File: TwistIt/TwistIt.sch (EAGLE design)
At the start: 13 parts

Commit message: Fix small things for Servo and Twistit
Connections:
- net P2: now also R2.1
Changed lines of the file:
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@@
 <segment>
 <pinref part="ST1" gate="G$1" pin="P$3"/>
-<wire x1="139.7" y1="99.06" x2="129.54" y2="99.06" width="0.1524" layer="91"/>
+<wire x1="139.7" y1="99.06" x2="121.92" y2="99.06" width="0.1524" layer="91"/>
 <label x="137.16" y="99.06" size="1.778" layer="95"/>
+<pinref part="R2" gate="G$1" pin="1"/>
 </segment>
 <segment>

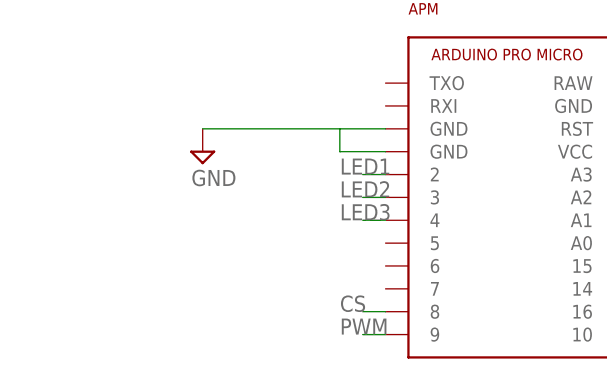
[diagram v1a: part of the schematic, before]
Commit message: Add encoder, start adding bom info to library
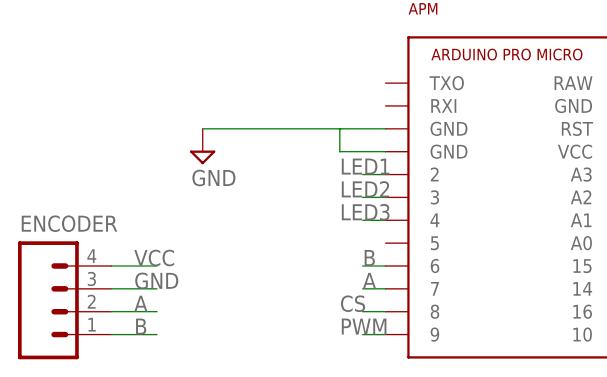
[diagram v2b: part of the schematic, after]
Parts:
- added ENCODER: (no value), pie:M041X04-MTA
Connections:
- new net A: APM.7, ENCODER.2
- new net B: APM.6, ENCODER.1
- net GND: now also ENCODER.3
- net VCC: now also ENCODER.4
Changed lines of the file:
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@@
 <part name="R6" library="pie" deviceset="R-US_" device="R0603" value="330"/>
 <part name="SUPPLY6" library="pie" deviceset="GND" device=""/>
+<part name="ENCODER" library="pie" deviceset="M04" device="1X04-MTA"/>
 </parts>
 <sheets>
@@
 <instance part="R6" gate="G$1" x="99.06" y="139.7"/>
 <instance part="SUPPLY6" gate="GND" x="111.76" y="137.16"/>
+<instance part="ENCODER" gate="G$1" x="10.16" y="83.82"/>
 </instances>
 <busses>
@@
 <wire x1="104.14" y1="139.7" x2="111.76" y2="139.7" width="0.1524" layer="91"/>
 </segment>
+<segment>
+<pinref part="ENCODER" gate="G$1" pin="3"/>
+<wire x1="17.78" y1="83.82" x2="22.86" y2="83.82" width="0.1524" layer="91"/>
+<label x="20.32" y="83.82" size="1.778" layer="95"/>
+</segment>
 </net>
 <net name="P1" class="0">
@@
 <wire x1="139.7" y1="142.24" x2="134.62" y2="142.24" width="0.1524" layer="91"/>
 </segment>
+<segment>
+<pinref part="ENCODER" gate="G$1" pin="4"/>
+<wire x1="17.78" y1="86.36" x2="22.86" y2="86.36" width="0.1524" layer="91"/>
+<label x="20.32" y="86.36" size="1.778" layer="95"/>
+</segment>
 </net>
 <net name="P2" class="0">
@@
 </segment>
 </net>
+<net name="A" class="0">
+<segment>
+<pinref part="ENCODER" gate="G$1" pin="2"/>
+<wire x1="17.78" y1="81.28" x2="22.86" y2="81.28" width="0.1524" layer="91"/>
+<label x="20.32" y="81.28" size="1.778" layer="95"/>
+</segment>
+<segment>
+<pinref part="APM" gate="G$1" pin="7"/>
+<wire x1="48.26" y1="83.82" x2="45.72" y2="83.82" width="0.1524" layer="91"/>
+<label x="45.72" y="83.82" size="1.778" layer="95"/>
+</segment>
+</net>
+<net name="B" class="0">
+<segment>
+<pinref part="ENCODER" gate="G$1" pin="1"/>
+<wire x1="17.78" y1="78.74" x2="22.86" y2="78.74" width="0.1524" layer="91"/>
+<label x="20.32" y="78.74" size="1.778" layer="95"/>
+</segment>
+<segment>
+<pinref part="APM" gate="G$1" pin="6"/>
+<wire x1="48.26" y1="86.36" x2="45.72" y2="86.36" width="0.1524" layer="91"/>
+<label x="45.72" y="86.36" size="1.778" layer="95"/>
+</segment>
+</net>

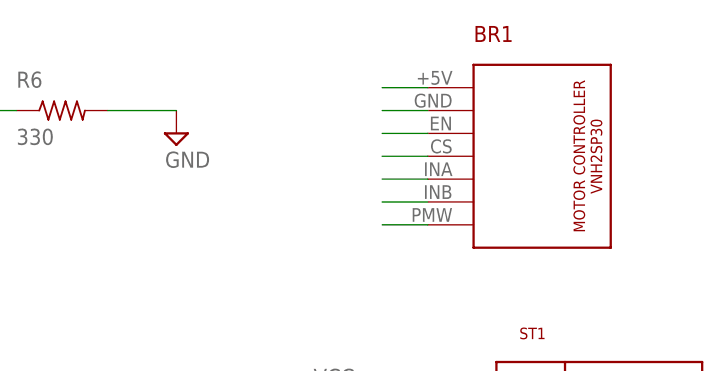
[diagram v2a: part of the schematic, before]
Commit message: Add more info to lbr; remove 5V from motor controlle rbreakout on twistit
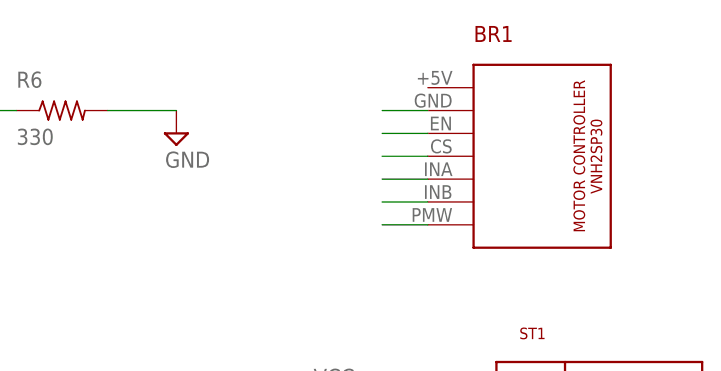
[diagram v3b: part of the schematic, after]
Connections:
- net VCC: no longer BR1.+5V
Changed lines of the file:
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@@
-</segment>
-<segment>
-<pinref part="BR1" gate="G$1" pin="+5V"/>
-<wire x1="139.7" y1="142.24" x2="134.62" y2="142.24" width="0.1524" layer="91"/>
 </segment>
 <segment>

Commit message: Readd the 5V rail on vhns
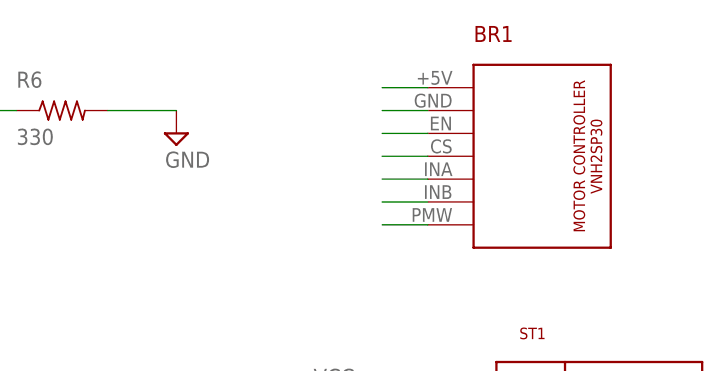
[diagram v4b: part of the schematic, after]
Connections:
- net VCC: now also BR1.+5V
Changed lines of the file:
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@@
 <label x="20.32" y="86.36" size="1.778" layer="95"/>
+</segment>
+<segment>
+<pinref part="BR1" gate="G$1" pin="+5V"/>
+<wire x1="139.7" y1="142.24" x2="134.62" y2="142.24" width="0.1524" layer="91"/>
 </segment>
 </net>

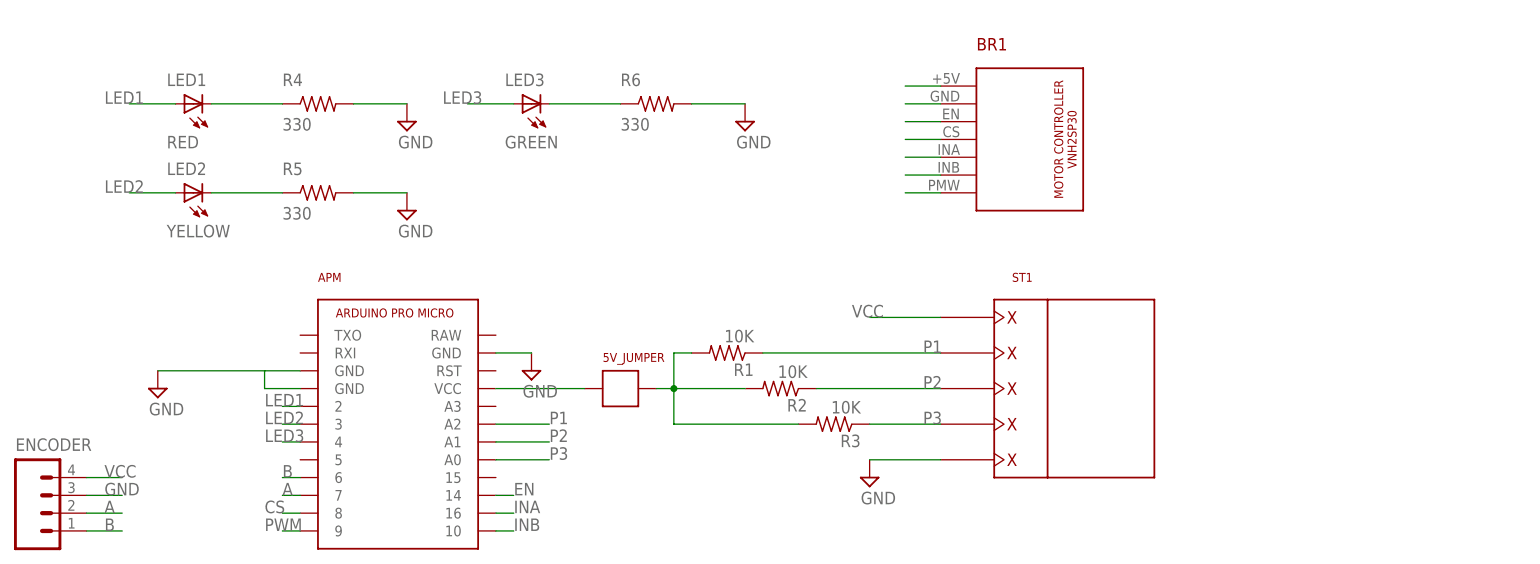
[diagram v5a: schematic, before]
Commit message: Rearange encoder to account for pullout and update parts
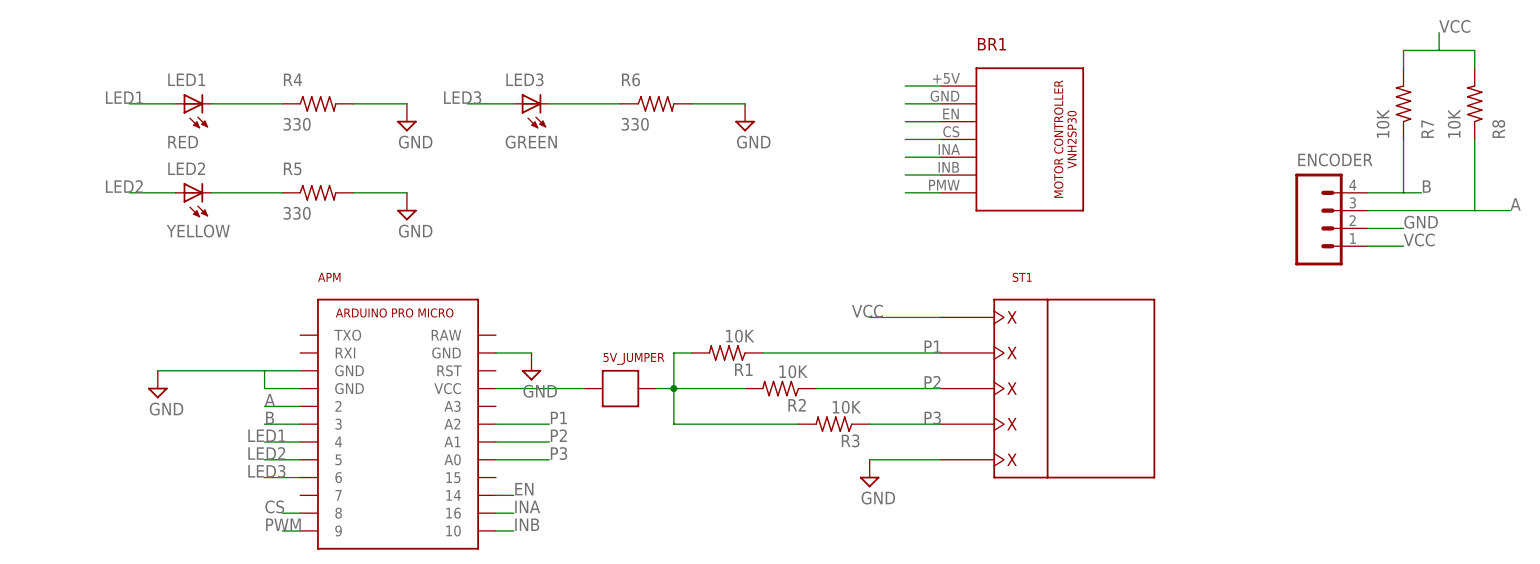
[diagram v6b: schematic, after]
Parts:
- added R7, R8: 10K, pie:R-US_R0603
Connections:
- net A: now also APM.2, ENCODER.3, R8.1; no longer APM.7, ENCODER.2
- net B: now also APM.3, ENCODER.4, R7.1; no longer APM.6, ENCODER.1
- net GND: now also ENCODER.2; no longer ENCODER.3
- net LED1: now also APM.4; no longer APM.2
- net LED2: now also APM.5; no longer APM.3
- net LED3: now also APM.6; no longer APM.4
- net VCC: now also ENCODER.1, R7.2, R8.2; no longer ENCODER.4
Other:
- moved on the sheet: ENCODER
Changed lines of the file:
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@@
 <part name="SUPPLY6" library="pie" deviceset="GND" device=""/>
 <part name="ENCODER" library="pie" deviceset="M04" device="1X04-MTA"/>
+<part name="R7" library="pie" deviceset="R-US_" device="R0603" value="10K"/>
+<part name="R8" library="pie" deviceset="R-US_" device="R0603" value="10K"/>
 </parts>
 <sheets>
@@
 <instance part="R6" gate="G$1" x="99.06" y="139.7"/>
 <instance part="SUPPLY6" gate="GND" x="111.76" y="137.16"/>
-<instance part="ENCODER" gate="G$1" x="10.16" y="83.82"/>
+<instance part="ENCODER" gate="G$1" x="193.04" y="124.46"/>
+<instance part="R7" gate="G$1" x="205.74" y="139.7" rot="MR90"/>
+<instance part="R8" gate="G$1" x="215.9" y="139.7" rot="MR90"/>
 </instances>
 <busses>
@@
 </segment>
 <segment>
-<pinref part="ENCODER" gate="G$1" pin="3"/>
-<wire x1="17.78" y1="83.82" x2="22.86" y2="83.82" width="0.1524" layer="91"/>
-<label x="20.32" y="83.82" size="1.778" layer="95"/>
+<pinref part="ENCODER" gate="G$1" pin="2"/>
+<wire x1="200.66" y1="121.92" x2="205.74" y2="121.92" width="0.1524" layer="91"/>
+<label x="205.74" y="121.92" size="1.778" layer="95"/>
 </segment>
 </net>
@@
 </segment>
 <segment>
-<pinref part="ENCODER" gate="G$1" pin="4"/>
-<wire x1="17.78" y1="86.36" x2="22.86" y2="86.36" width="0.1524" layer="91"/>
-<label x="20.32" y="86.36" size="1.778" layer="95"/>
-</segment>
-<segment>
 <pinref part="BR1" gate="G$1" pin="+5V"/>
 <wire x1="139.7" y1="142.24" x2="134.62" y2="142.24" width="0.1524" layer="91"/>
+</segment>
+<segment>
+<pinref part="ENCODER" gate="G$1" pin="1"/>
+<wire x1="200.66" y1="119.38" x2="205.74" y2="119.38" width="0.1524" layer="91"/>
+<label x="205.74" y="119.38" size="1.778" layer="95"/>
+</segment>
+<segment>
+<pinref part="R7" gate="G$1" pin="2"/>
+<wire x1="205.74" y1="144.78" x2="205.74" y2="147.32" width="0.1524" layer="91"/>
+<label x="210.82" y="149.86" size="1.778" layer="95"/>
+<pinref part="R8" gate="G$1" pin="2"/>
+<wire x1="215.9" y1="144.78" x2="215.9" y2="147.32" width="0.1524" layer="91"/>
+<wire x1="205.74" y1="147.32" x2="210.82" y2="147.32" width="0.1524" layer="91"/>
+<wire x1="210.82" y1="147.32" x2="215.9" y2="147.32" width="0.1524" layer="91"/>
+<wire x1="210.82" y1="147.32" x2="210.82" y2="149.86" width="0.1524" layer="91"/>
 </segment>
 </net>
@@
 </segment>
 <segment>
-<pinref part="APM" gate="APM" pin="2"/>
-<wire x1="48.26" y1="96.52" x2="45.72" y2="96.52" width="0.1524" layer="91"/>
-<label x="43.18" y="96.52" size="1.778" layer="95"/>
+<pinref part="APM" gate="APM" pin="4"/>
+<wire x1="48.26" y1="91.44" x2="43.18" y2="91.44" width="0.1524" layer="91"/>
+<label x="40.64" y="91.44" size="1.778" layer="95"/>
 </segment>
 </net>
@@
 </segment>
 <segment>
-<pinref part="APM" gate="APM" pin="3"/>
-<wire x1="48.26" y1="93.98" x2="45.72" y2="93.98" width="0.1524" layer="91"/>
-<label x="43.18" y="93.98" size="1.778" layer="95"/>
+<pinref part="APM" gate="APM" pin="5"/>
+<wire x1="48.26" y1="88.9" x2="43.18" y2="88.9" width="0.1524" layer="91"/>
+<label x="40.64" y="88.9" size="1.778" layer="95"/>
 </segment>
 </net>
@@
 </segment>
 <segment>
-<pinref part="APM" gate="APM" pin="4"/>
-<wire x1="48.26" y1="91.44" x2="45.72" y2="91.44" width="0.1524" layer="91"/>
-<label x="43.18" y="91.44" size="1.778" layer="95"/>
+<pinref part="APM" gate="APM" pin="6"/>
+<wire x1="48.26" y1="86.36" x2="43.18" y2="86.36" width="0.1524" layer="91"/>
+<label x="40.64" y="86.36" size="1.778" layer="95"/>
 </segment>
 </net>
@@
 <net name="A" class="0">
 <segment>
-<pinref part="ENCODER" gate="G$1" pin="2"/>
-<wire x1="17.78" y1="81.28" x2="22.86" y2="81.28" width="0.1524" layer="91"/>
-<label x="20.32" y="81.28" size="1.778" layer="95"/>
-</segment>
-<segment>
-<pinref part="APM" gate="APM" pin="7"/>
-<wire x1="48.26" y1="83.82" x2="45.72" y2="83.82" width="0.1524" layer="91"/>
-<label x="45.72" y="83.82" size="1.778" layer="95"/>
+<pinref part="APM" gate="APM" pin="2"/>
+<wire x1="48.26" y1="96.52" x2="43.18" y2="96.52" width="0.1524" layer="91"/>
+<label x="43.18" y="96.52" size="1.778" layer="95"/>
+</segment>
+<segment>
+<pinref part="ENCODER" gate="G$1" pin="3"/>
+<wire x1="200.66" y1="124.46" x2="215.9" y2="124.46" width="0.1524" layer="91"/>
+<label x="220.98" y="124.46" size="1.778" layer="95"/>
+<pinref part="R8" gate="G$1" pin="1"/>
+<wire x1="215.9" y1="124.46" x2="220.98" y2="124.46" width="0.1524" layer="91"/>
+<wire x1="215.9" y1="134.62" x2="215.9" y2="124.46" width="0.1524" layer="91"/>
 </segment>
 </net>
 <net name="B" class="0">
 <segment>
-<pinref part="ENCODER" gate="G$1" pin="1"/>
-<wire x1="17.78" y1="78.74" x2="22.86" y2="78.74" width="0.1524" layer="91"/>
-<label x="20.32" y="78.74" size="1.778" layer="95"/>
-</segment>
-<segment>
-<pinref part="APM" gate="APM" pin="6"/>
-<wire x1="48.26" y1="86.36" x2="45.72" y2="86.36" width="0.1524" layer="91"/>
-<label x="45.72" y="86.36" size="1.778" layer="95"/>
-</segment>
-</net>
+<pinref part="APM" gate="APM" pin="3"/>
+<wire x1="48.26" y1="93.98" x2="43.18" y2="93.98" width="0.1524" layer="91"/>
+<label x="43.18" y="93.98" size="1.778" layer="95"/>
+</segment>
+<segment>
+<pinref part="ENCODER" gate="G$1" pin="4"/>
+<wire x1="200.66" y1="127" x2="205.74" y2="127" width="0.1524" layer="91"/>
+<label x="208.28" y="127" size="1.778" layer="95"/>
+<pinref part="R7" gate="G$1" pin="1"/>
+<wire x1="205.74" y1="127" x2="208.28" y2="127" width="0.1524" layer="91"/>
+<wire x1="205.74" y1="134.62" x2="205.74" y2="127" width="0.1524" layer="91"/>
+</segment>
+</net>

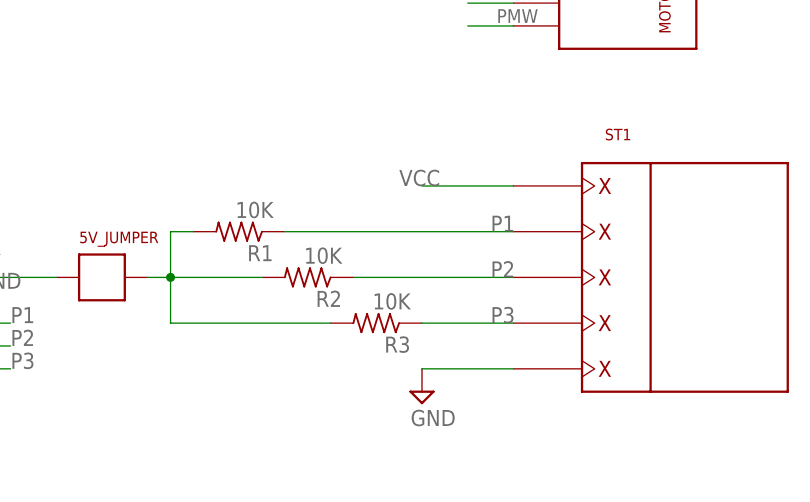
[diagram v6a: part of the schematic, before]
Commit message: Unmirror screw terminal, relabel LEDs
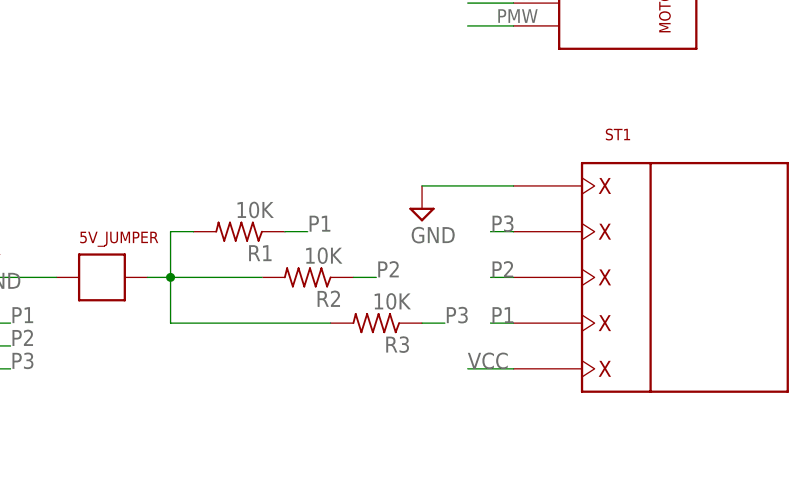
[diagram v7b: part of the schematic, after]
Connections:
- net GND: now also ST1.P$1; no longer ST1.P$5
- net P1: now also ST1.P$4; no longer ST1.P$2
- net P3: now also ST1.P$2; no longer ST1.P$4
- net VCC: now also ST1.P$5; no longer ST1.P$1
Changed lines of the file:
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@@
 <instance part="SUPPLY2" gate="GND" x="27.94" y="99.06"/>
 <instance part="ST1" gate="G$1" x="160.02" y="99.06"/>
-<instance part="SUPPLY1" gate="GND" x="129.54" y="86.36"/>
+<instance part="SUPPLY1" gate="GND" x="129.54" y="106.68"/>
 <instance part="SUPPLY3" gate="GND" x="81.28" y="101.6"/>
 <instance part="5V_JUMPER" gate="G$1" x="93.98" y="99.06"/>
@@
 </segment>
 <segment>
-<pinref part="ST1" gate="G$1" pin="P$5"/>
-<wire x1="139.7" y1="88.9" x2="129.54" y2="88.9" width="0.1524" layer="91"/>
-<pinref part="SUPPLY1" gate="GND" pin="GND"/>
-</segment>
-<segment>
 <pinref part="SUPPLY3" gate="GND" pin="GND"/>
 <pinref part="APM" gate="APM" pin="GND@2"/>
@@
 <label x="205.74" y="121.92" size="1.778" layer="95"/>
 </segment>
+<segment>
+<pinref part="SUPPLY1" gate="GND" pin="GND"/>
+<pinref part="ST1" gate="G$1" pin="P$1"/>
+<wire x1="129.54" y1="109.22" x2="139.7" y2="109.22" width="0.1524" layer="91"/>
+</segment>
 </net>
 <net name="P1" class="0">
-<segment>
-<pinref part="ST1" gate="G$1" pin="P$2"/>
-<label x="137.16" y="104.14" size="1.778" layer="95"/>
-<pinref part="R1" gate="G$1" pin="1"/>
-<wire x1="114.3" y1="104.14" x2="139.7" y2="104.14" width="0.1524" layer="91"/>
-</segment>
 <segment>
 <pinref part="APM" gate="APM" pin="A2"/>
@@
 <label x="83.82" y="93.98" size="1.778" layer="95"/>
 </segment>
+<segment>
+<pinref part="R1" gate="G$1" pin="1"/>
+<wire x1="114.3" y1="104.14" x2="116.84" y2="104.14" width="0.1524" layer="91"/>
+<label x="116.84" y="104.14" size="1.778" layer="95"/>
+</segment>
+<segment>
+<pinref part="ST1" gate="G$1" pin="P$4"/>
+<wire x1="139.7" y1="93.98" x2="137.16" y2="93.98" width="0.1524" layer="91"/>
+<label x="137.16" y="93.98" size="1.778" layer="95"/>
+</segment>
 </net>
 <net name="VCC" class="0">
-<segment>
-<pinref part="ST1" gate="G$1" pin="P$1"/>
-<wire x1="139.7" y1="109.22" x2="129.54" y2="109.22" width="0.1524" layer="91"/>
-<label x="127" y="109.22" size="1.778" layer="95"/>
-</segment>
 <segment>
 <pinref part="APM" gate="APM" pin="VCC"/>
@@
 <wire x1="210.82" y1="147.32" x2="210.82" y2="149.86" width="0.1524" layer="91"/>
 </segment>
+<segment>
+<pinref part="ST1" gate="G$1" pin="P$5"/>
+<wire x1="139.7" y1="88.9" x2="134.62" y2="88.9" width="0.1524" layer="91"/>
+<label x="134.62" y="88.9" size="1.778" layer="95"/>
+</segment>
 </net>
 <net name="P2" class="0">
-<segment>
-<pinref part="ST1" gate="G$1" pin="P$3"/>
-<wire x1="139.7" y1="99.06" x2="121.92" y2="99.06" width="0.1524" layer="91"/>
-<label x="137.16" y="99.06" size="1.778" layer="95"/>
-<pinref part="R2" gate="G$1" pin="1"/>
-</segment>
 <segment>
 <pinref part="APM" gate="APM" pin="A1"/>
@@
 <label x="83.82" y="91.44" size="1.778" layer="95"/>
 </segment>
+<segment>
+<pinref part="R2" gate="G$1" pin="1"/>
+<wire x1="121.92" y1="99.06" x2="124.46" y2="99.06" width="0.1524" layer="91"/>
+<label x="124.46" y="99.06" size="1.778" layer="95"/>
+</segment>
+<segment>
+<pinref part="ST1" gate="G$1" pin="P$3"/>
+<wire x1="139.7" y1="99.06" x2="137.16" y2="99.06" width="0.1524" layer="91"/>
+<label x="137.16" y="99.06" size="1.778" layer="95"/>
+</segment>
 </net>
 <net name="P3" class="0">
-<segment>
-<pinref part="ST1" gate="G$1" pin="P$4"/>
-<wire x1="139.7" y1="93.98" x2="129.54" y2="93.98" width="0.1524" layer="91"/>
-<label x="137.16" y="93.98" size="1.778" layer="95"/>
-<pinref part="R3" gate="G$1" pin="1"/>
-</segment>
 <segment>
 <pinref part="APM" gate="APM" pin="A0"/>
@@
 <label x="83.82" y="88.9" size="1.778" layer="95"/>
 </segment>
+<segment>
+<pinref part="R3" gate="G$1" pin="1"/>
+<wire x1="129.54" y1="93.98" x2="132.08" y2="93.98" width="0.1524" layer="91"/>
+<label x="132.08" y="93.98" size="1.778" layer="95"/>
+</segment>
+<segment>
+<pinref part="ST1" gate="G$1" pin="P$2"/>
+<wire x1="139.7" y1="104.14" x2="137.16" y2="104.14" width="0.1524" layer="91"/>
+<label x="137.16" y="104.14" size="1.778" layer="95"/>
+</segment>
 </net>
